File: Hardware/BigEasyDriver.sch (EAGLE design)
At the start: 55 parts, among them IC1 A4983ALT1, IC2 LM317L

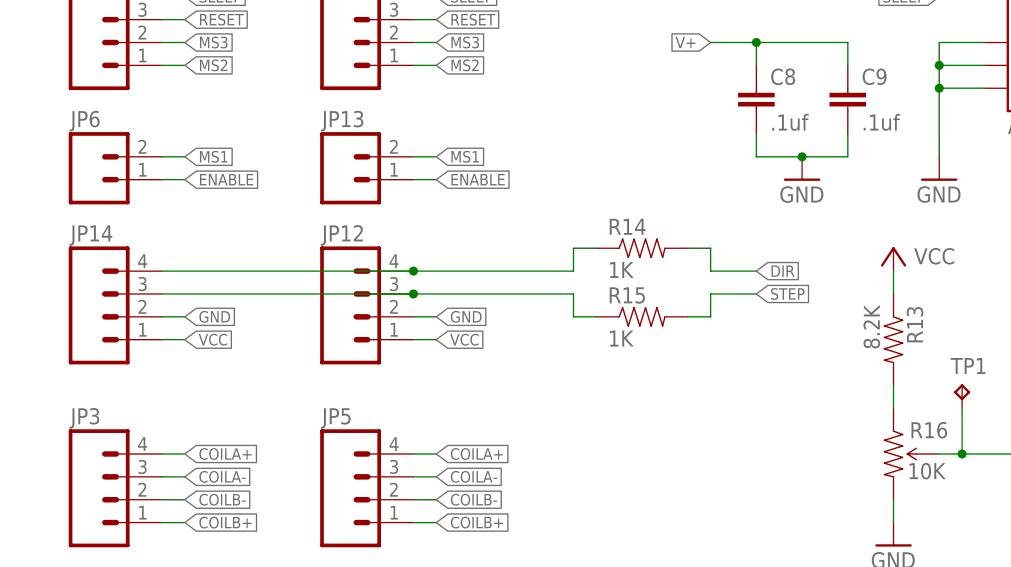
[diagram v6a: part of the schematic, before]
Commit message: Updated STEP and DIR inputs schematic net wires so they are not as confusing.
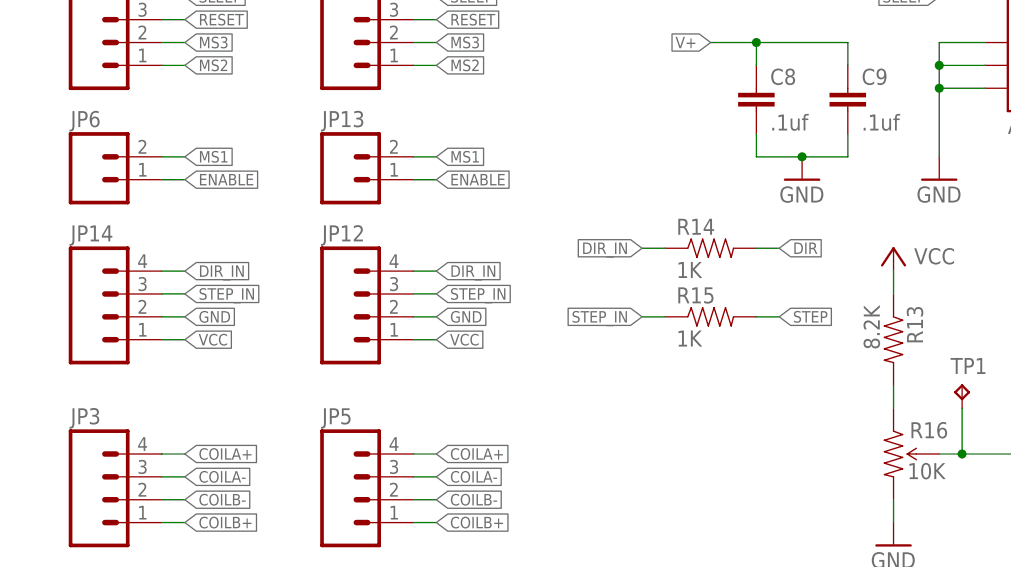
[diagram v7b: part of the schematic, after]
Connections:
- net N$55 renamed DIR_IN
- net N$56 renamed STEP_IN
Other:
- moved on the sheet: R14, R15
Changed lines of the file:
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@@
 <setting verticaltext="up"/>
 </settings>
-<grid distance="0.1" unitdist="inch" unit="inch" style="lines" multiple="1" display="no" altdistance="0.05" altunitdist="inch" altunit="inch"/>
+<grid distance="0.1" unitdist="inch" unit="inch" style="lines" multiple="1" display="no" altdistance="0.01" altunitdist="inch" altunit="inch"/>
 <layers>
 <layer number="1" name="Top" color="4" fill="1" visible="no" active="no"/>
@@
 <instance part="U$4" gate="G$1" x="185.42" y="121.92"/>
 <instance part="U$5" gate="G$1" x="185.42" y="119.38"/>
-<instance part="R14" gate="G$1" x="109.22" y="101.6"/>
-<instance part="R15" gate="G$1" x="109.22" y="93.98"/>
+<instance part="R14" gate="G$1" x="116.84" y="101.6"/>
+<instance part="R15" gate="G$1" x="116.84" y="93.98"/>
 </instances>
 <busses>
@@
 </segment>
 <segment>
-<wire x1="116.84" y1="99.06" x2="121.92" y2="99.06" width="0.1524" layer="91"/>
+<wire x1="121.92" y1="101.6" x2="124.46" y2="101.6" width="0.1524" layer="91"/>
 <pinref part="R14" gate="G$1" pin="2"/>
-<wire x1="114.3" y1="101.6" x2="116.84" y2="101.6" width="0.1524" layer="91"/>
-<wire x1="116.84" y1="101.6" x2="116.84" y2="99.06" width="0.1524" layer="91"/>
-<label x="121.92" y="99.06" size="1.27" layer="95" xref="yes"/>
+<label x="124.46" y="101.6" size="1.27" layer="95" xref="yes"/>
 </segment>
 </net>
@@
 </segment>
 <segment>
-<wire x1="116.84" y1="96.52" x2="121.92" y2="96.52" width="0.1524" layer="91"/>
-<wire x1="116.84" y1="93.98" x2="116.84" y2="96.52" width="0.1524" layer="91"/>
+<wire x1="121.92" y1="93.98" x2="124.46" y2="93.98" width="0.1524" layer="91"/>
 <pinref part="R15" gate="G$1" pin="2"/>
-<wire x1="114.3" y1="93.98" x2="116.84" y2="93.98" width="0.1524" layer="91"/>
-<label x="121.92" y="96.52" size="1.27" layer="95" xref="yes"/>
+<label x="124.46" y="93.98" size="1.27" layer="95" xref="yes"/>
 </segment>
 </net>
@@
 </segment>
 </net>
-<net name="N$55" class="0">
+<net name="DIR_IN" class="0">
+<segment>
+<pinref part="R14" gate="G$1" pin="1"/>
+<wire x1="111.76" y1="101.6" x2="109.22" y2="101.6" width="0.1524" layer="91"/>
+<label x="109.22" y="101.6" size="1.27" layer="95" rot="R180" xref="yes"/>
+</segment>
 <segment>
 <pinref part="JP14" gate="G$1" pin="4"/>
-<wire x1="83.82" y1="99.06" x2="101.6" y2="99.06" width="0.1524" layer="91"/>
+<wire x1="55.88" y1="99.06" x2="58.42" y2="99.06" width="0.1524" layer="91"/>
+<label x="58.42" y="99.06" size="1.27" layer="95" xref="yes"/>
+</segment>
+<segment>
+<wire x1="83.82" y1="99.06" x2="86.36" y2="99.06" width="0.1524" layer="91"/>
 <pinref part="JP12" gate="G$1" pin="4"/>
-<wire x1="55.88" y1="99.06" x2="83.82" y2="99.06" width="0.1524" layer="91"/>
-<junction x="83.82" y="99.06"/>
-<pinref part="R14" gate="G$1" pin="1"/>
-<wire x1="104.14" y1="101.6" x2="101.6" y2="101.6" width="0.1524" layer="91"/>
-<wire x1="101.6" y1="101.6" x2="101.6" y2="99.06" width="0.1524" layer="91"/>
-</segment>
-</net>
-<net name="N$56" class="0">
+<label x="86.36" y="99.06" size="1.27" layer="95" xref="yes"/>
+</segment>
+</net>
+<net name="STEP_IN" class="0">
+<segment>
+<wire x1="83.82" y1="96.52" x2="86.36" y2="96.52" width="0.1524" layer="91"/>
+<pinref part="JP12" gate="G$1" pin="3"/>
+<label x="86.36" y="96.52" size="1.27" layer="95" xref="yes"/>
+</segment>
 <segment>
 <pinref part="JP14" gate="G$1" pin="3"/>
-<wire x1="83.82" y1="96.52" x2="101.6" y2="96.52" width="0.1524" layer="91"/>
-<pinref part="JP12" gate="G$1" pin="3"/>
-<wire x1="55.88" y1="96.52" x2="83.82" y2="96.52" width="0.1524" layer="91"/>
-<junction x="83.82" y="96.52"/>
+<wire x1="55.88" y1="96.52" x2="58.42" y2="96.52" width="0.1524" layer="91"/>
+<label x="58.42" y="96.52" size="1.27" layer="95" xref="yes"/>
+</segment>
+<segment>
 <pinref part="R15" gate="G$1" pin="1"/>
-<wire x1="104.14" y1="93.98" x2="101.6" y2="93.98" width="0.1524" layer="91"/>
-<wire x1="101.6" y1="93.98" x2="101.6" y2="96.52" width="0.1524" layer="91"/>
-</segment>
-</net>
+<wire x1="111.76" y1="93.98" x2="109.22" y2="93.98" width="0.1524" layer="91"/>
+<label x="109.22" y="93.98" size="1.27" layer="95" rot="R180" xref="yes"/>
+</segment>
+</net>

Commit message: Updating part package w/ Sparkle IDs
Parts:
- C1, C11, C6, C7, C8, C9: device SparkFun:CAP0603-CAP -> SparkFun-Capacitors:0.1UF-100V-10%(0603)
- C10: device SparkFun:CAP0603-CAP -> SparkFun-Capacitors:0.22UF50V-20%,+80%(0603)
- C14: device SparkFun:CAP_POLD -> SparkFun-Capacitors:47UF-50V-20%(ELECT)
- C2: device SparkFun:CAP0603-CAP -> SparkFun-Capacitors:1.0UF-16V-10%(0603)
- R1, R10, R11, R12, R2, R20, R3, R4, R5: device SparkFun:RESISTOR0603-RES -> SparkFun-Resistors:20KOHM1/10W5%(0603)
- R13: device SparkFun:RESISTOR0603-RES -> SparkFun-Resistors:8.2KOHM-1/10W-5%(0603)
- R14, R15, R9: device SparkFun:RESISTOR0603-RES -> SparkFun-Resistors:1KOHM1/10W1%(0603)
- R18, R19: device SparkFun:RESISTOR2010 -> SparkFun-Resistors:0.11OHM1/2W1%(2010)
- R6: device SparkFun:RESISTOR0603-RES -> SparkFun-Resistors:390OHM1/10W1%(0603)
- R7: device SparkFun:RESISTOR0603-RES -> SparkFun-Resistors:330OHM1/10W1%(0603)
- R8: device SparkFun:RESISTOR0603-RES -> SparkFun-Resistors:240OHM1/10W1%(0603)
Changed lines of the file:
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@@
 <?xml version="1.0" encoding="utf-8"?>
 <!DOCTYPE eagle SYSTEM "eagle.dtd">
-<eagle version="6.4">
+<eagle version="6.5.0">
 <drawing>
 <settings>
@@
 <part name="GND1" library="supply1" deviceset="GND" device=""/>
 <part name="FRAME1" library="SparkFun-Aesthetics" deviceset="FRAME-LETTER" device=""/>
-<part name="R6" library="SparkFun" deviceset="RESISTOR" device="0603-RES" value="390"/>
-<part name="R8" library="SparkFun" deviceset="RESISTOR" device="0603-RES" value="240"/>
+<part name="R6" library="SparkFun-Resistors" deviceset="390OHM1/10W1%(0603)" device="" value="390"/>
+<part name="R8" library="SparkFun-Resistors" deviceset="240OHM1/10W1%(0603)" device="" value="240"/>
 <part name="PWR_LED" library="SparkFun03_30_09" deviceset="LED" device="0603" value="YELLOW"/>
-<part name="R9" library="SparkFun" deviceset="RESISTOR" device="0603-RES" value="1K"/>
+<part name="R9" library="SparkFun-Resistors" deviceset="1KOHM1/10W1%(0603)" device="" value="1K"/>
 <part name="P+1" library="supply1" deviceset="+5V" device="" value="VCC"/>
-<part name="C1" library="SparkFun" deviceset="CAP" device="0603-CAP" value=".1uF"/>
+<part name="C1" library="SparkFun-Capacitors" deviceset="0.1UF-100V-10%(0603)" device="" value=".1uF"/>
 <part name="IC2" library="BigEasyDriver_v11" deviceset="SPARKFUN03_30_09_V_REG_317" device="SOT89" technology="SOT89" value="LM317L"/>
 <part name="APWR" library="SparkFun03_30_09" deviceset="SOLDERJUMPER" device="TRACE"/>
 <part name="3/5V" library="SparkFun03_30_09" deviceset="SOLDERJUMPER" device="NO"/>
-<part name="R7" library="SparkFun" deviceset="RESISTOR" device="0603-RES" value="330"/>
+<part name="R7" library="SparkFun-Resistors" deviceset="330OHM1/10W1%(0603)" device="" value="330"/>
 <part name="R16" library="SparkFun-Electromechanical" deviceset="TRIMPOT" device="3MM-2" value="10K"/>
 <part name="GND4" library="supply1" deviceset="GND" device=""/>
@@
 <part name="JP1" library="SparkFun" deviceset="M02" device="PTH"/>
 <part name="GND19" library="supply1" deviceset="GND" device=""/>
-<part name="R18" library="SparkFun" deviceset="RESISTOR" device="2010" value=".11"/>
-<part name="R19" library="SparkFun" deviceset="RESISTOR" device="2010" value=".11"/>
+<part name="R18" library="SparkFun-Resistors" deviceset="0.11OHM1/2W1%(2010)" device="" value=".11"/>
+<part name="R19" library="SparkFun-Resistors" deviceset="0.11OHM1/2W1%(2010)" device="" value=".11"/>
 <part name="IC1" library="Testing" deviceset="A4983" device="ALT1"/>
 <part name="GND16" library="supply1" deviceset="GND" device=""/>
-<part name="R20" library="SparkFun" deviceset="RESISTOR" device="0603-RES" value="20K"/>
+<part name="R20" library="SparkFun-Resistors" deviceset="20KOHM1/10W5%(0603)" device="" value="20K"/>
 <part name="GND17" library="supply1" deviceset="GND" device=""/>
-<part name="C6" library="SparkFun" deviceset="CAP" device="0603-CAP" value=".1uf"/>
-<part name="C7" library="SparkFun" deviceset="CAP" device="0603-CAP" value=".1uf"/>
+<part name="C6" library="SparkFun-Capacitors" deviceset="0.1UF-100V-10%(0603)" device="" value=".1uf"/>
+<part name="C7" library="SparkFun-Capacitors" deviceset="0.1UF-100V-10%(0603)" device="" value=".1uf"/>
 <part name="GND18" library="supply1" deviceset="GND" device=""/>
 <part name="P+2" library="SparkFun-2-11-09" deviceset="VCC" device=""/>
-<part name="C8" library="SparkFun" deviceset="CAP" device="0603-CAP" value=".1uf"/>
-<part name="C9" library="SparkFun" deviceset="CAP" device="0603-CAP" value=".1uf"/>
+<part name="C8" library="SparkFun-Capacitors" deviceset="0.1UF-100V-10%(0603)" device="" value=".1uf"/>
+<part name="C9" library="SparkFun-Capacitors" deviceset="0.1UF-100V-10%(0603)" device="" value=".1uf"/>
 <part name="GND20" library="supply1" deviceset="GND" device=""/>
-<part name="C10" library="SparkFun" deviceset="CAP" device="0603-CAP" value=".22uF"/>
-<part name="C11" library="SparkFun" deviceset="CAP" device="0603-CAP" value=".1uf"/>
+<part name="C10" library="SparkFun-Capacitors" deviceset="0.22UF50V-20%,+80%(0603)" device="" value=".22uF"/>
+<part name="C11" library="SparkFun-Capacitors" deviceset="0.1UF-100V-10%(0603)" device="" value=".1uf"/>
 <part name="D1" library="diode" deviceset="DIODE-" device="DO-214AC" value="B340A-13-F"/>
-<part name="C14" library="SparkFun" deviceset="CAP_POL" device="D" value="47uF"/>
+<part name="C14" library="SparkFun-Capacitors" deviceset="47UF-50V-20%(ELECT)" device="" value="47uF"/>
 <part name="JP10" library="SparkFun" deviceset="M04" device="PTH"/>
 <part name="JP5" library="BigEasyDriver_v11" deviceset="M04" device="SCREW_LOCK"/>
 <part name="JP7" library="BigEasyDriver_v11" deviceset="M02" device="3.5MM_LOCK"/>
-<part name="R1" library="SparkFun" deviceset="RESISTOR" device="0603-RES" value="20K"/>
-<part name="R2" library="SparkFun" deviceset="RESISTOR" device="0603-RES" value="20K"/>
-<part name="R3" library="SparkFun" deviceset="RESISTOR" device="0603-RES" value="20K"/>
-<part name="R4" library="SparkFun" deviceset="RESISTOR" device="0603-RES" value="20K"/>
-<part name="R5" library="SparkFun" deviceset="RESISTOR" device="0603-RES" value="20K"/>
+<part name="R1" library="SparkFun-Resistors" deviceset="20KOHM1/10W5%(0603)" device="" value="20K"/>
+<part name="R2" library="SparkFun-Resistors" deviceset="20KOHM1/10W5%(0603)" device="" value="20K"/>
+<part name="R3" library="SparkFun-Resistors" deviceset="20KOHM1/10W5%(0603)" device="" value="20K"/>
+<part name="R4" library="SparkFun-Resistors" deviceset="20KOHM1/10W5%(0603)" device="" value="20K"/>
+<part name="R5" library="SparkFun-Resistors" deviceset="20KOHM1/10W5%(0603)" device="" value="20K"/>
 <part name="P+3" library="SparkFun-2-11-09" deviceset="VCC" device=""/>
 <part name="GND3" library="supply1" deviceset="GND" device=""/>
-<part name="R10" library="SparkFun" deviceset="RESISTOR" device="0603-RES" value="20K"/>
-<part name="R11" library="SparkFun" deviceset="RESISTOR" device="0603-RES" value="20K"/>
-<part name="R12" library="SparkFun" deviceset="RESISTOR" device="0603-RES" value="20K"/>
-<part name="R13" library="SparkFun" deviceset="RESISTOR" device="0603-RES" value="8.2K"/>
+<part name="R10" library="SparkFun-Resistors" deviceset="20KOHM1/10W5%(0603)" device="" value="20K"/>
+<part name="R11" library="SparkFun-Resistors" deviceset="20KOHM1/10W5%(0603)" device="" value="20K"/>
+<part name="R12" library="SparkFun-Resistors" deviceset="20KOHM1/10W5%(0603)" device="" value="20K"/>
+<part name="R13" library="SparkFun-Resistors" deviceset="8.2KOHM-1/10W-5%(0603)" device="" value="8.2K"/>
 <part name="JP11" library="BigEasyDriver_v11" deviceset="M04" device="SCREW_LOCK"/>
 <part name="JP12" library="BigEasyDriver_v11" deviceset="M04" device="SCREW_LOCK"/>
 <part name="JP13" library="BigEasyDriver_v11" deviceset="M02" device="3.5MM_LOCK"/>
 <part name="JP14" library="SparkFun" deviceset="M04" device="PTH"/>
-<part name="C2" library="SparkFun" deviceset="CAP" device="0603-CAP" value="1uF"/>
+<part name="C2" library="SparkFun-Capacitors" deviceset="1.0UF-16V-10%(0603)" device="" value="1uF"/>
 <part name="LOGO1" library="OSHW" deviceset="OSHW_LOGO_FILL" device="X0100-NT"/>
 <part name="JP2" library="abes" deviceset="FIDUCIAL" device="1X2.5"/>
@@
 <part name="U$4" library="Testing" deviceset="PAD" device=""/>
 <part name="U$5" library="Testing" deviceset="PAD" device=""/>
-<part name="R14" library="SparkFun" deviceset="RESISTOR" device="0603-RES" value="1K"/>
-<part name="R15" library="SparkFun" deviceset="RESISTOR" device="0603-RES" value="1K"/>
+<part name="R14" library="SparkFun-Resistors" deviceset="1KOHM1/10W1%(0603)" device="" value="1K"/>
+<part name="R15" library="SparkFun-Resistors" deviceset="1KOHM1/10W1%(0603)" device="" value="1K"/>
 </parts>
 <sheets>
